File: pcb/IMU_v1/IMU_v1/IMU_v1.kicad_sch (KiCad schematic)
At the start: 7 parts, among them J1 Conn_01x08

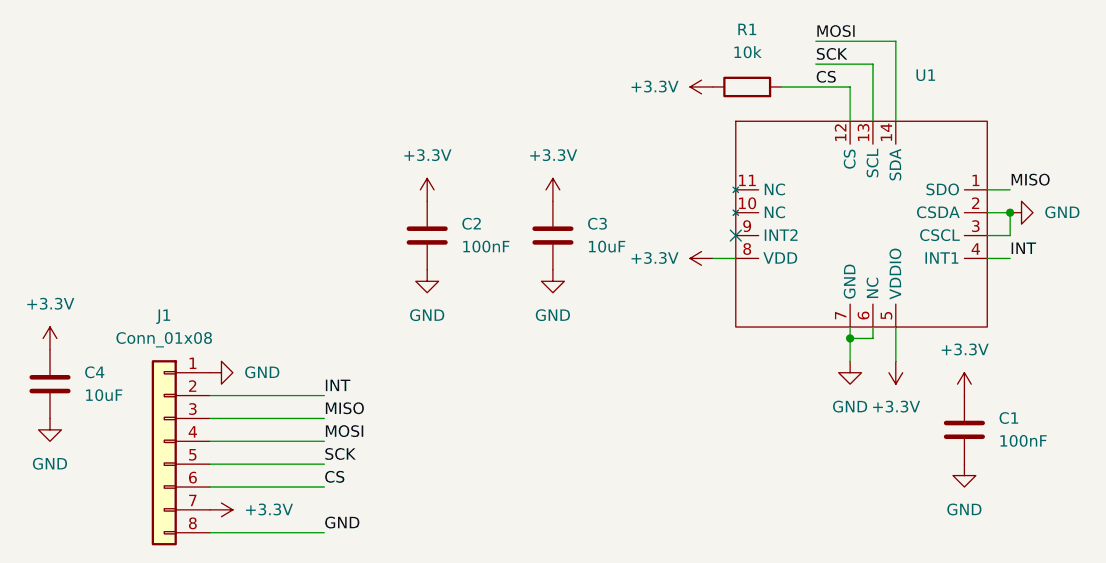
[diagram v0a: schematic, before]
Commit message: made new imu project and added symbols/footprint
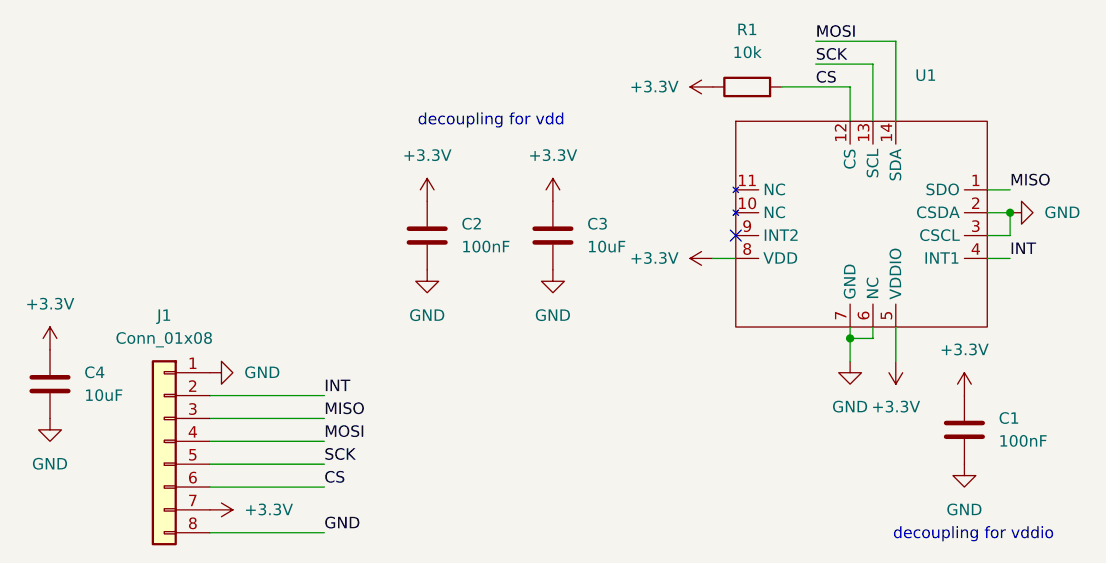
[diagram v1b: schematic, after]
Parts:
- U1: value ~ -> (none)
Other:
- note added: "decoupling for vdd"
- note added: "decoupling for vddio"
